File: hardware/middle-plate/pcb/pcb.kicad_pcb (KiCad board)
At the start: 2 copper layers, 218 x 205.7 mm, 119 parts, among them SW1 MT-0-102-A101-M200-RS+PJ, SW2 TS4535TP 250GF 009, SW3 TS4535TP 250GF 009, SW4 TS4535TP 250GF 009, SW5 TS4535TP 250GF 009, SW6 TS4535TP 250GF 009, SW7 TS4535TP 250GF 009

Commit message: label a bunch
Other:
- board text added: "3V3"
- board text added: "5V"
- board text added: "GND"
- board text added: "MOSI"
- board text added: "MOSO"
- board text added: "PCM .CLK"
- board text added: "PCM .DIN"
- board text added: "PCM .FS"
- board text added: "PWM0"
- board text added: "PWM1"
- board text added: "SCL"
- board text added: "SCS0"
- board text added: "SCS1"
- board text added: "SDA"
- board text added: "SLCK"

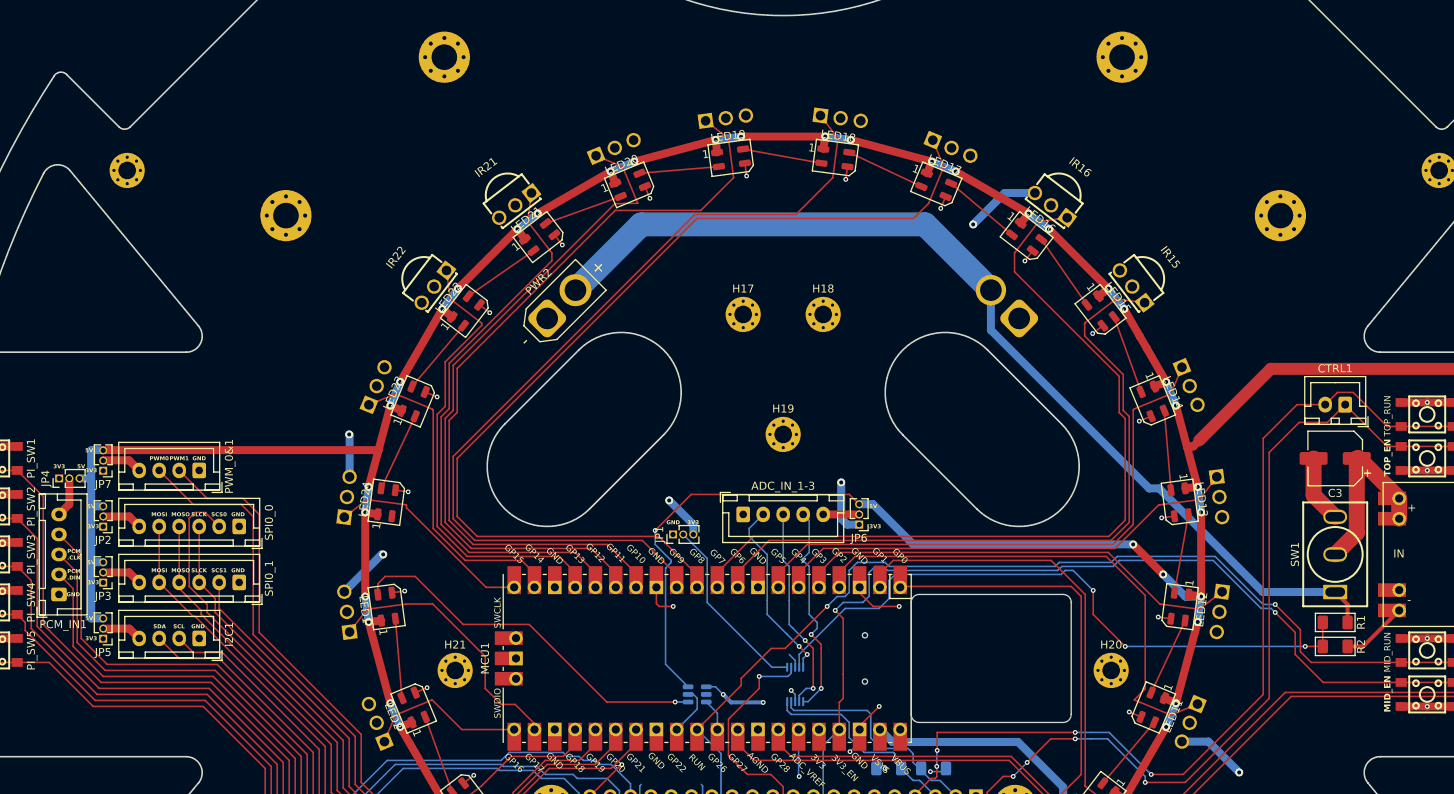
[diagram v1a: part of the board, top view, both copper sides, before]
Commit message: labelled bottom middle and top pcbs, added testpoints
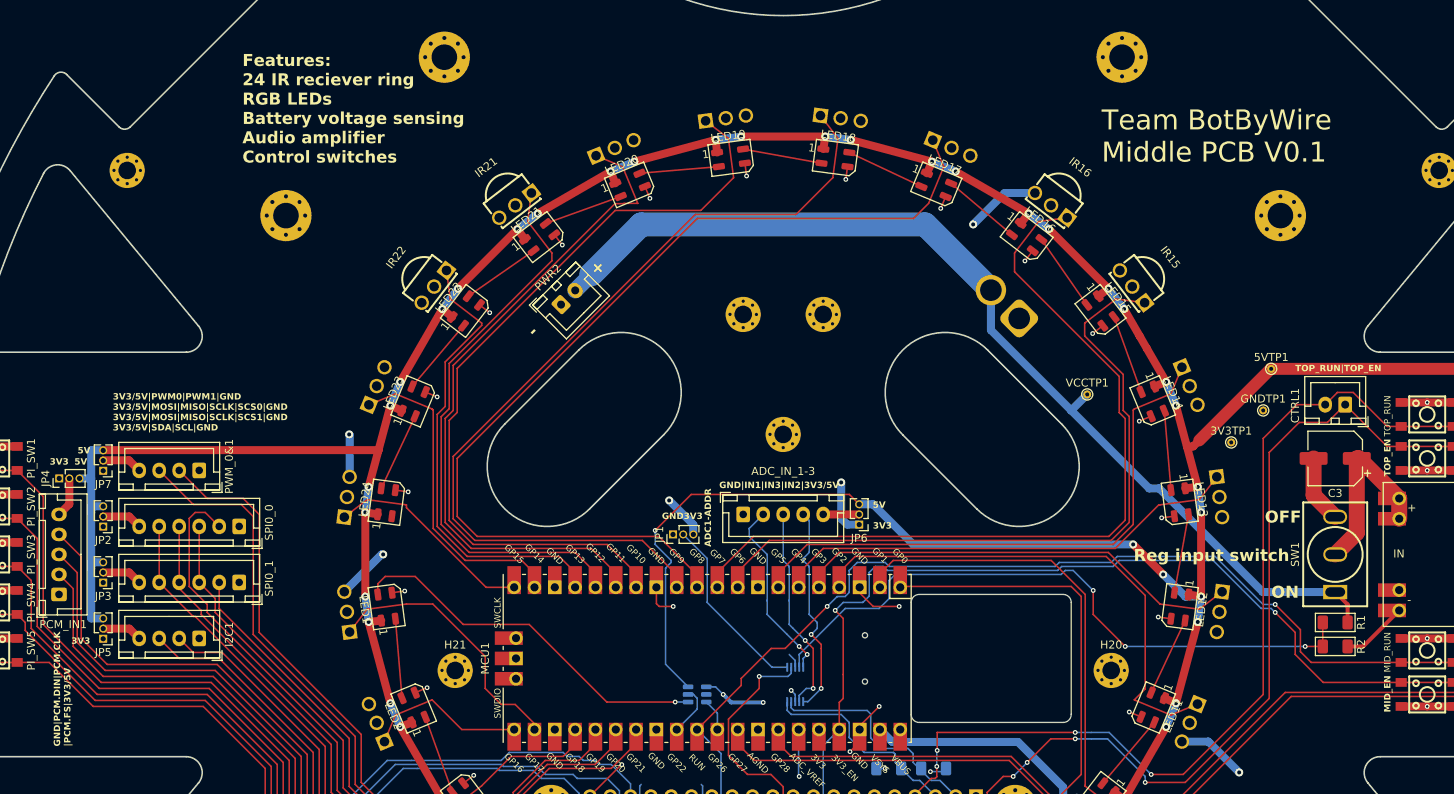
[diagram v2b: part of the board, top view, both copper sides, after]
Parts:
- added 3V3TP1: TestPoint, TestPoint:TestPoint_THTPad_D1.0mm_Drill0.5mm, F.Cu at (56.0, -14.0)
- added 5VTP1: TestPoint, TestPoint:TestPoint_THTPad_D1.0mm_Drill0.5mm, F.Cu at (61.0, -23.2)
- added GNDTP1: TestPoint, TestPoint:TestPoint_THTPad_D1.0mm_Drill0.5mm, F.Cu at (60.0, -18.0)
- added VCCTP1: TestPoint, TestPoint:TestPoint_THTPad_D1.0mm_Drill0.5mm, F.Cu at (38.0, -20.0)
- PWR2: value XT30-F -> Conn_01x02; footprint Connector_AMASS:AMASS_XT30U-F_1x02_P5.0mm_Vertical -> Connector_JST:JST_XH_B2B-XH-A_1x02_P2.50mm_Vertical
- moved PWR2 2.45 mm to (-27.8, -31.2)
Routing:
- net VCC: track 124.8 -> 127.6 mm
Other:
- board text added: "+"
- board text added: "-"
- board text added: "3V3/5V|PWM0|PWM1|GND 3V3/5V|MOSI|MISO|SCLK|SCS0|GND 3V3/5V|MOSI|MISO|SCLK|SCS1|GND 3V3/5V|SDA|SCL|GND"
- board text added: "ADC1-ADDR"
- board text added: "Features: 24 IR reciever ring RGB LEDs Battery voltage sensing Audio amplifier Control switches"
- board text added: "GND|IN1|IN3|IN2|3V3/5V"
- board text added: "GND|PCM.DIN|PCM.CLK |PCM.FS|3V3/5V"
- board text added: "OFF"
- board text added: "ON"
- board text added: "Reg input switch"
- board text added: "TOP_RUN|TOP_EN"
- board text added: "Team BotByWire Middle PCB V0.1"
- board text removed: "MOSI"
- board text removed: "MOSO"
- board text removed: "PCM .CLK"
- board text removed: "PCM .DIN"
- board text removed: "PCM .FS"
- board text removed: "PWM0"
- board text removed: "PWM1"
- board text removed: "SCL"
- board text removed: "SCS0"
- board text removed: "SCS1"
- board text removed: "SDA"
- board text removed: "SLCK"
